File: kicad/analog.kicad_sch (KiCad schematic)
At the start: 22 parts, among them J25 pH probe, J26 pH module, J27 AIN3, U5 ADS1115IDGSR, U6 TLV9062IDR, U7 TL431BCDBZR

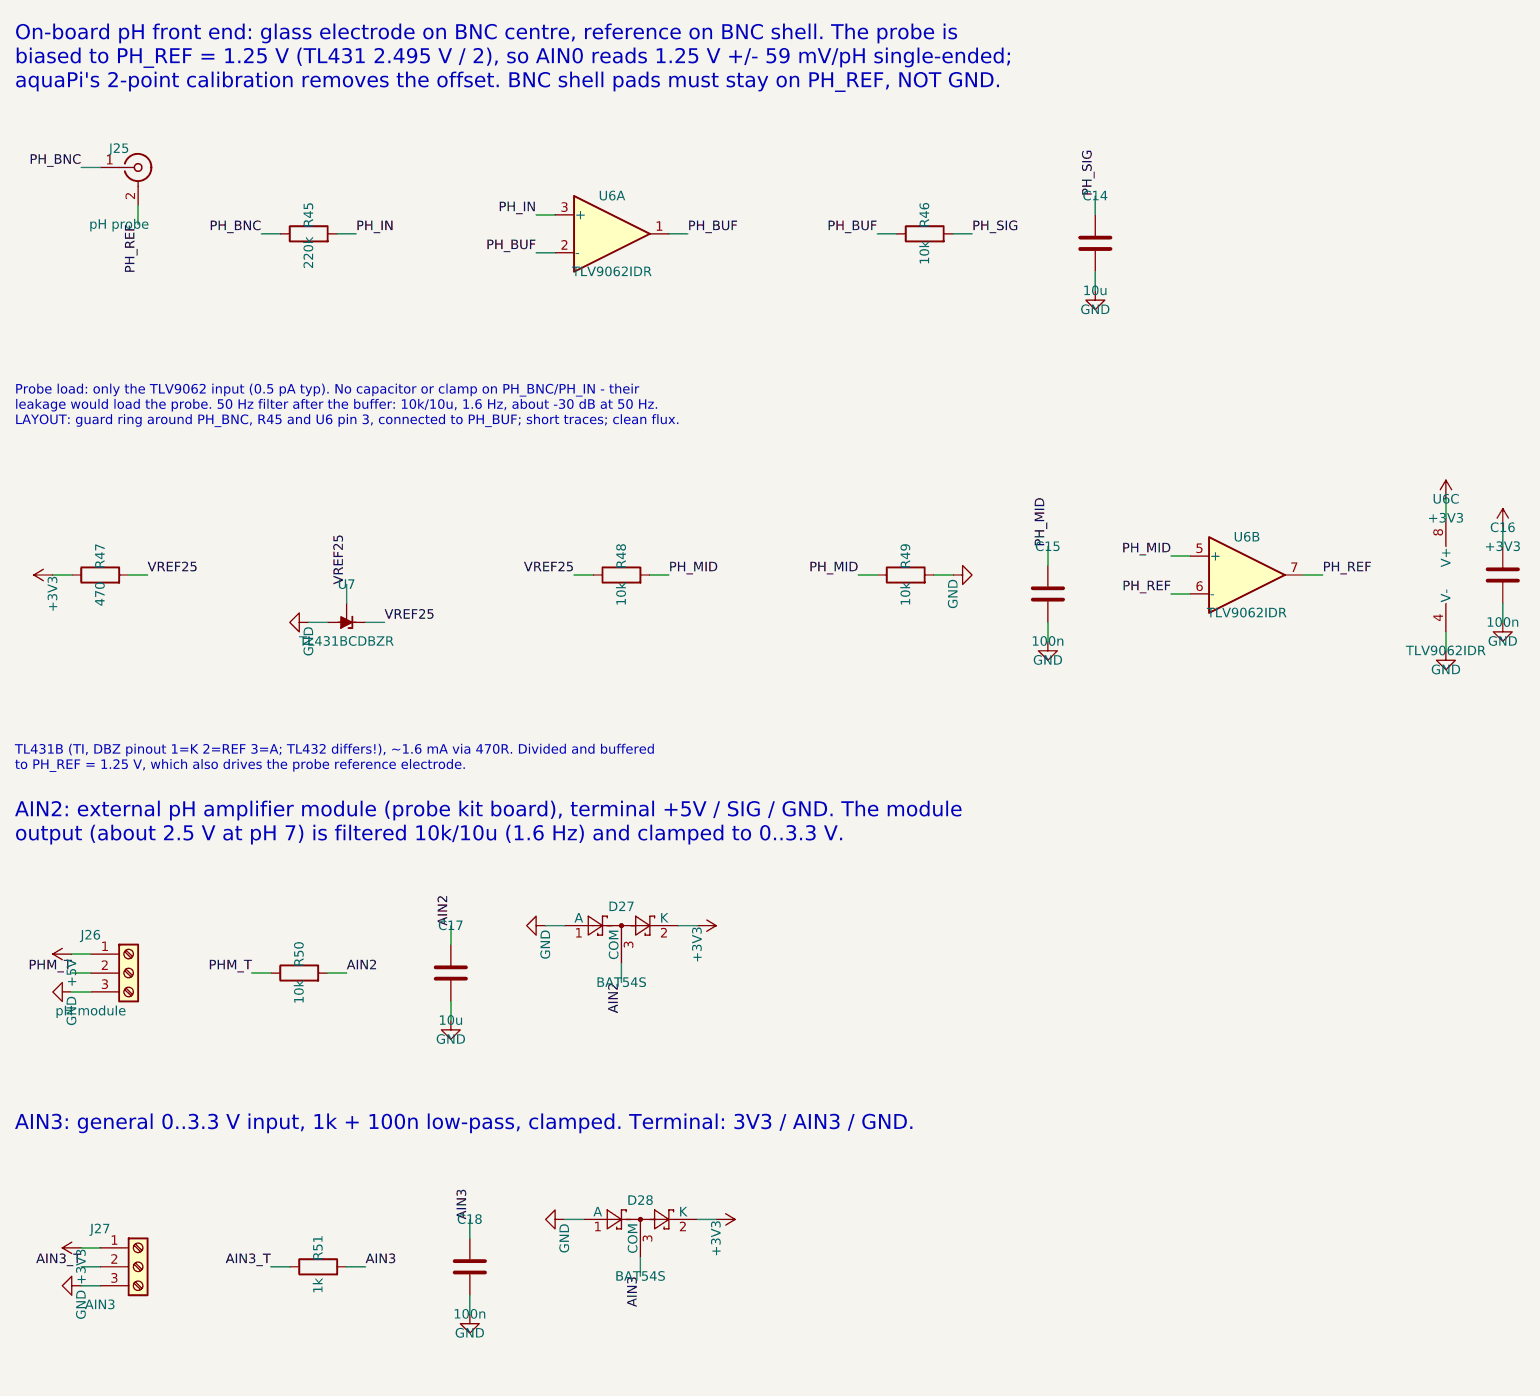
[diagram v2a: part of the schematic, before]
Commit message: kicad: styroflex filter capacitor across the pH probe
Polystyrene film leaks far less than an MLCC, so the input filter can
stay without loading the probe: 2.2 nF from PH_IN to PH_REF, with the
electrode resistance a 0.2..2 s filter against pump 50 Hz. Hand-soldered
axial part from Reichelt; BOM, README and cost estimate updated.

Co-Authored-By: Claude Opus 5.5 <noreply@anthropic.com>
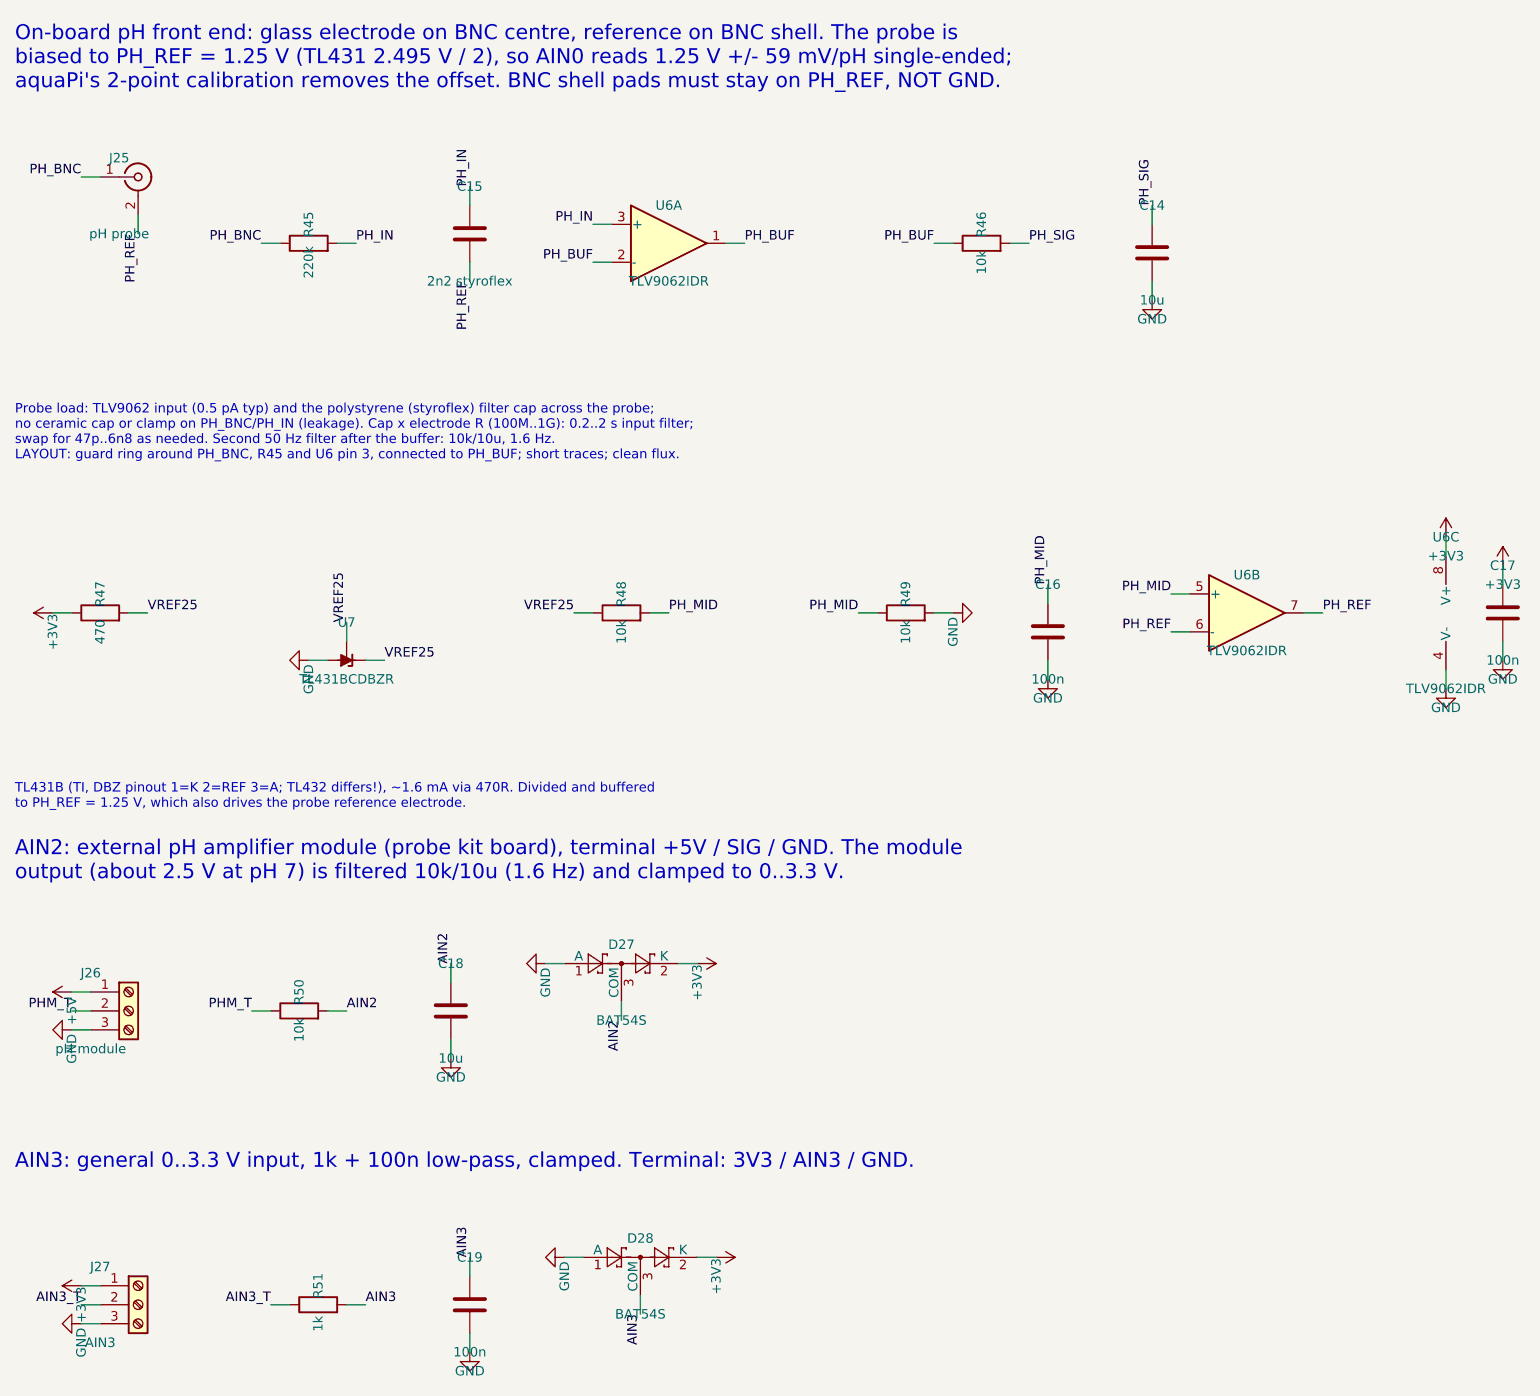
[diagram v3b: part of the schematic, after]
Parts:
- added C19: 100n, Capacitor_SMD:C_0805_2012Metric, symbol Device:C
- C15: value 100n -> 2n2 styroflex; footprint Capacitor_SMD:C_0805_2012Metric -> Capacitor_THT:C_Axial_L12.0mm_D6.5mm_P15.00mm_Horizontal; LCSC C49678 -> (none); Reichelt (none) -> STYROFLEX 2,2N
- C17: value 10u -> 100n; LCSC C15850 -> C49678
- C18: value 100n -> 10u; LCSC C49678 -> C15850
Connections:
- net +3V3: now also C17.1; no longer C16.1
- net AIN2: now also C18.1; no longer C17.1
- net AIN3: now also C19.1; no longer C18.1
- net GND: now also C19.2; no longer C15.2
- net PH_IN: now also C15.1
- net PH_MID: now also C16.1; no longer C15.1
- net PH_REF: now also C15.2
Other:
- note added: "Probe load: TLV9062 input (0.5 pA typ) and the polystyrene (styroflex) filter cap across the probe; no ceramic cap or clamp on PH_BNC/PH_IN (leakage). Cap x electrode R (100M..1G): 0.2..2 s input filter; swap for 47p..6n8 as needed. Second 50 Hz filter after the buffer: 10k/10u, 1.6 Hz. LAYOUT: guard ring around PH_BNC, R45 and U6 pin 3, connected to PH_BUF; short traces; clean flux."
- note removed: "Probe load: only the TLV9062 input (0.5 pA typ). No capacitor or clamp on PH_BNC/PH_IN - their leakage would load the probe. 50 Hz filter after the buffer: 10k/10u, 1.6 Hz, about -30 dB at 50 Hz. LAYOUT: guard ring around PH_BNC, R45 and U6 pin 3, connected to PH_BUF; short traces; clean flux."

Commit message: kicad: galvanically isolate the analog / pH section
The tank water is tied to board GND through other sensors (DS18B20
sleeve), so the biased pH reference electrode would carry a continuous
DC current. Move ADS1115, pH buffer, TL431 and the AIN2/AIN3 terminals
to an isolated domain: B0505S 1 W DC/DC + AMS1117 for ISO_3V3, ISO1540
I2C isolator (side 2 on the Pi bus, side 1 on the ADS1115). Netlist
checked: only the DC/DC and the ISO1540 cross the boundary. BOM, README
and cost estimate (~45 EUR/board at 5) updated.

Co-Authored-By: Claude Opus 5.5 <noreply@anthropic.com>
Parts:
- removed U5: ADS1115IDGSR, Package_SO:TSSOP-10_3x3mm_P0.5mm, symbol Analog_ADC:ADS1115IDGS
- removed U6: TLV9062IDR, Package_SO:SOIC-8_3.9x4.9mm_P1.27mm, symbol Amplifier_Operational:TLV9062xD
- removed U7: TL431BCDBZR, Package_TO_SOT_SMD:SOT-23, symbol Reference_Voltage:TL431DBZ
- added C20, C24: 10u, Capacitor_SMD:C_0805_2012Metric, symbol Device:C
- added C21: 2n2 styroflex, Capacitor_THT:C_Axial_L12.0mm_D6.5mm_P15.00mm_Horizontal, symbol Device:C
- added C22, C23, C25: 100n, Capacitor_SMD:C_0805_2012Metric, symbol Device:C
- added R52, R53: 10k, Resistor_SMD:R_0805_2012Metric, symbol Device:R
- added R54: 1k, Resistor_SMD:R_0805_2012Metric, symbol Device:R
- added U10: TL431BCDBZR, Package_TO_SOT_SMD:SOT-23, symbol Reference_Voltage:TL431DBZ
- added U5: B0505S-1WR3, Converter_DCDC:Converter_DCDC_Murata_CRE1xxxxxxSC_THT, symbol Converter_DCDC_Isolated:CRE1S0505SC
- added U6: AMS1117-3.3, Package_TO_SOT_SMD:SOT-223-3_TabPin2, symbol Regulator_Linear:AMS1117-3.3
- added U7: ISO1540DR, Package_SO:SOIC-8_3.9x4.9mm_P1.27mm, symbol Isolator:ISO1540
- added U8: ADS1115IDGSR, Package_SO:TSSOP-10_3x3mm_P0.5mm, symbol Analog_ADC:ADS1115IDGS
- added U9: TLV9062IDR, Package_SO:SOIC-8_3.9x4.9mm_P1.27mm, symbol Amplifier_Operational:TLV9062xD
- C13, C16: value 100n -> 10u; LCSC C49678 -> C15850
- C15: value 2n2 styroflex -> 10u; footprint Capacitor_THT:C_Axial_L12.0mm_D6.5mm_P15.00mm_Horizontal -> Capacitor_SMD:C_0805_2012Metric; LCSC (none) -> C15850; Reichelt STYROFLEX 2,2N -> (none)
- C18: value 10u -> 100n; LCSC C15850 -> C49678
- R45: value 220k -> 1k; LCSC C17556 -> C17513
- R46: value 10k -> 4k7; LCSC C17414 -> C17673
- R47: value 470 -> 4k7; LCSC C17710 -> C17673
- R48: value 10k -> 220k; LCSC C17414 -> C17556
- R50: value 10k -> 470; LCSC C17414 -> C17710
- R51: value 1k -> 10k; LCSC C17513 -> C17414
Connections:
- net +3V3: now also C18.1, U7.8 (VCC2); no longer C13.1, C17.1, D27.2 (K), D28.2 (K), J27.1 (Pin_1), JP4.3 (B), R47.1
- net +5V: now also C13.1, U5.2 (+VIN); no longer J26.1 (Pin_1)
- net ADS_ADDR: now also U8.1 (ADDR)
- net AIN2: now also C24.1, R53.2, U8.6 (AIN2); no longer C18.1, R50.2
- net AIN3: now also C25.1, R54.2, U8.7 (AIN3); no longer C19.1, R51.2
- net AIN3_T: now also R54.1; no longer R51.1
- net GND: now also U5.1 (-VIN), U7.5 (GND2); no longer C14.2, C16.2, C17.2, C19.2, D27.1 (A), D28.1 (A), J26.3 (Pin_3), J27.3 (Pin_3), JP4.1 (A), R49.2
- net GPIO2_SDA: now also U7.7 (SDA2)
- net GPIO3_SCL: now also U7.6 (SCL2)
- net PHM_T: now also R53.1; no longer R50.1
- net PH_BNC: now also R48.1; no longer R45.1
- net PH_BUF: now also R49.1, U9.1, U9.2 (-); no longer R46.1
- net PH_IN: now also R48.2, C21.1, U9.3 (+); no longer C15.1, R45.2
- net PH_MID: now also R51.2, C22.1, R52.1, U9.5 (+); no longer C16.1, R48.2, R49.1
- net PH_REF: now also C21.2, U8.5 (AIN1), U9.6 (-), U9.7; no longer C15.2
- net PH_SIG: now also R49.2, C20.1, U8.4 (AIN0); no longer C14.1, R46.2
- net VREF25: now also R50.2, R51.1, U10.1 (K), U10.2 (REF); no longer R47.2, R48.1
- new net ISO_3V3: C16.1, C17.1, C19.1, C23.1, D27.2 (K), D28.2 (K), J27.1 (Pin_1), JP4.3 (B), R46.1, R47.1, R50.1, U6.2 (VO), U7.1 (VCC1), U8.8 (VDD), U9.8 (V+)
- new net ISO_5V: C14.1, C15.1, J26.1 (Pin_1), R45.1, U5.4 (+VOUT), U6.3 (VI)
- new net ISO_GND: C14.2, C15.2, C16.2, C17.2, C19.2, C20.2, C22.2, C23.2, C24.2, C25.2, D27.1 (A), D28.1 (A), J26.3 (Pin_3), J27.3 (Pin_3), JP4.1 (A), R45.2, R52.2, U10.3 (A), U5.3 (-VOUT), U6.1 (GND), U7.4 (GND1), U8.3 (GND), U9.4 (V-)
- new net ISO_SCL: R47.2, U7.3 (SCL1), U8.10 (SCL)
- new net ISO_SDA: R46.2, U7.2 (SDA1), U8.9 (SDA)
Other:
- note added: "1W isolated DC/DC, 1 kV. 1k dummy load (5 mA) plus LDO quiescent current keep its output from rising at light load. ISO_5V also supplies the external pH module terminal."
- note added: "ADS1115 on ISO_3V3, I2C address 0x48 (JP 1-2, default) or 0x49 (2-3). ALERT/RDY unused. All channels are read single-ended (aquaPi driver): AIN0 on-board pH, AIN1 pH reference (monitor, allows AIN0-AIN1 differential later), AIN2 external pH amplifier module, AIN3 general."
- note added: "AIN2: external pH amplifier module (probe kit board), terminal ISO_5V / SIG / ISO_GND - isolated as well. Output (about 2.5 V at pH 7) filtered 10k/10u (1.6 Hz) and clamped to 0..3.3 V."
- note added: "AIN3: general 0..3.3 V input on the isolated side (sensor GND must be ISO_GND!), 1k + 100n, clamped. Terminal: ISO_3V3 / AIN3 / ISO_GND."
- note added: "ISO1540: side 2 (normal low level) on the Pi I2C bus; side 1 (low level 0.57..0.8 V) only drives the ADS1115 (V_IL 0.99 V at 3.3 V). Side-1 pull-ups 4k7 -> 0.7 mA, within the required 0.5..3.5 mA."
- note added: "Probe load: TLV9062 input (0.5 pA typ) and the polystyrene (styroflex) filter cap across the probe; no ceramic cap or clamp on PH_BNC/PH_IN (leakage). Cap x electrode R (100M..1G): 0.2..2 s input filter; swap for 47p..6n8 as needed. Second 50 Hz filter after the buffer: 10k/10u, 1.6 Hz. LAYOUT: guard ring around PH_BNC, R/C input parts and TLV9062 pin 3, connected to PH_BUF; slots; clean flux."
- note added: "The whole analog section is galvanically isolated (ISO_GND). The tank water is often tied to board GND through other sensors (e.g. a DS18B20 sleeve); without isolation a DC current would flow through the pH reference electrode and destroy it. LAYOUT: keep >= 2 mm (better a slot) between the GND and ISO_GND domains; only the B0505S DC/DC and the ISO1540 cross the gap."
- note removed: "ADS1115 on 3.3 V, I2C address 0x48 (JP 1-2, default) or 0x49 (2-3). ALERT/RDY unused. All channels are read single-ended (aquaPi driver): AIN0 on-board pH, AIN1 pH reference (monitor, allows AIN0-AIN1 differential later), AIN2 external pH amplifier module, AIN3 general."
- note removed: "AIN2: external pH amplifier module (probe kit board), terminal +5V / SIG / GND. The module output (about 2.5 V at pH 7) is filtered 10k/10u (1.6 Hz) and clamped to 0..3.3 V."
- note removed: "AIN3: general 0..3.3 V input, 1k + 100n low-pass, clamped. Terminal: 3V3 / AIN3 / GND."
- note removed: "Probe load: TLV9062 input (0.5 pA typ) and the polystyrene (styroflex) filter cap across the probe; no ceramic cap or clamp on PH_BNC/PH_IN (leakage). Cap x electrode R (100M..1G): 0.2..2 s input filter; swap for 47p..6n8 as needed. Second 50 Hz filter after the buffer: 10k/10u, 1.6 Hz. LAYOUT: guard ring around PH_BNC, R45 and U6 pin 3, connected to PH_BUF; short traces; clean flux."
- title: aquaPCB – ADS1115 ADC and pH front end -> aquaPCB – Isolated ADC and pH front end
